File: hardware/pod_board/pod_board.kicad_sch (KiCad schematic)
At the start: 77 parts, among them J1 USB-C, J2 IMU (BNO085 breakout), J3 GNSS (NEO-M8N breakout), J4 Gesture puck (JST-GH), J5 SWD (ST-Link), J6 ELM327 fallback (USART3), J7 DB-25 to power box, SW1 RESET, SW2 BOOT, U1 STM32F405RGT6, U3 AP2112K-3.3, U4 USBLC6-2SC6, Y1 8MHz

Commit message: Power board schematic redrawn as wired sheets under a block diagram
kisheet.py writes hierarchical KiCad sheets with parts placed by hand and
wires routed between pins; power_board_drawing.py lays out eight function
sheets and the root block diagram. check.sh also builds the label-only
version and requires identical netlists (compare_nets.py).

Fixes check_nets.py reading no components from KiCad 10 netlists, which
made the footprint check pass with nothing to check.
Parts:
- removed R31, R33: 100, Resistor_SMD:R_0805_2012Metric, symbol Device:R
- removed R31, R32, R33: 1k, Resistor_SMD:R_0805_2012Metric, symbol Device:R
- removed R32: 10k, Resistor_SMD:R_0805_2012Metric, symbol Device:R
- added R31, R32, R33: 1k, Resistor_SMD:R_0805_2012Metric, symbol Device:R
- added R31, R33: 100, Resistor_SMD:R_0805_2012Metric, symbol Device:R
- added R32: 10k, Resistor_SMD:R_0805_2012Metric, symbol Device:R
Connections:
- net +3V3: now also R32.1
- net CAN_RX: now also R31.2
- net HX711_DOUT: now also R33.2
- net LED_ARMED: now also R32.1
- net LED_ARMED_A: now also R32.2
- net LED_FAULT: now also R33.1
- net LED_FAULT_A: now also R33.2
- net LED_LINK: now also R31.1
- net LED_LINK_A: now also R31.2
- net X_CAN_RX: now also R31.1, R32.2
- net X_HX711_DOUT: now also R33.1

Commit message: Pod board schematic redrawn as wired sheets; duplicate references fixed
pod_board_drawing.py draws six sheets around an MCU sheet under a block
diagram; check.sh now compares both boards' drawn and label-only netlists.
kisheet.py: stacked pins, PWR_FLAGs on signal nets, column hints for
crossing-free fan-ins, nets drawn in pieces joined by name, and visible
rail names on power symbols.

R31-R33 were used twice on the pod board, which KiCad's ERC does not
report; the netlist merged each pair. Cable parts now start at R40/C40,
generate.py rejects duplicate references and check_nets.py fails on a pin
in two nets. check_nets.py also drops the sheet path from net names.
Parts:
- removed C1, C2: 10u, Capacitor_SMD:C_1206_3216Metric, symbol Device:C
- removed C10, C11: 2.2u, Capacitor_SMD:C_0805_2012Metric, symbol Device:C
- removed C12, C13: 15p, Capacitor_SMD:C_0805_2012Metric, symbol Device:C
- removed C14, C3, C35, C4, C5, C6, C9: 100n, Capacitor_SMD:C_0805_2012Metric, symbol Device:C
- removed C15: 4.7n, Capacitor_SMD:C_0805_2012Metric, symbol Device:C
- removed C24, C27, C30: 10n, Capacitor_SMD:C_0805_2012Metric, symbol Device:C
- removed C7: 4.7u, Capacitor_SMD:C_1206_3216Metric, symbol Device:C
- removed C8: 1u, Capacitor_SMD:C_0805_2012Metric, symbol Device:C
- removed D1, D2: SS14, Diode_SMD:D_SMA, symbol Device:D_Schottky
- removed D3: green, LED_SMD:LED_0805_2012Metric, symbol Device:LED
- removed D4: blue, LED_SMD:LED_0805_2012Metric, symbol Device:LED
- removed D5: amber, LED_SMD:LED_0805_2012Metric, symbol Device:LED
- removed D6: red, LED_SMD:LED_0805_2012Metric, symbol Device:LED
- removed H1, H2, H3, H4: M3, MountingHole:MountingHole_3.2mm_M3, symbol Mechanical:MountingHole
- removed J1: USB-C, Connector_USB:USB_C_Receptacle_HRO_TYPE-C-31-M-12, symbol Connector:USB_C_Receptacle_USB2.0_16P
- removed J2: IMU (BNO085 breakout), Connector_PinHeader_2.54mm:PinHeader_1x06_P2.54mm_Vertical, symbol Connector_Generic:Conn_01x06
- removed J3: GNSS (NEO-M8N breakout), Connector_PinHeader_2.54mm:PinHeader_1x05_P2.54mm_Vertical, symbol Connector_Generic:Conn_01x05
- removed J4: Gesture puck (JST-GH), Connector_JST:JST_GH_SM05B-GHS-TB_1x05-1MP_P1.25mm_Horizontal, symbol Connector_Generic:Conn_01x05
- removed J5: SWD (ST-Link), Connector_PinHeader_2.54mm:PinHeader_1x05_P2.54mm_Vertical, symbol Connector_Generic:Conn_01x05
- removed J6: ELM327 fallback (USART3), Connector_PinHeader_2.54mm:PinHeader_1x04_P2.54mm_Vertical, symbol Connector_Generic:Conn_01x04
- removed J7: DB-25 to power box, Connector_Dsub:DSUB-25_Socket_Horizontal_P2.77x2.84mm_EdgePinOffset4.94mm_Housed_MountingHolesOffset4.94mm, symbol Connector:DB25_Socket_MountingHoles
- removed R1, R23, R26, R29, R32: 10k, Resistor_SMD:R_0805_2012Metric, symbol Device:R
- removed R10, R11, R12, R13, R14, R15, R16, R17, R18, R20, R21, R22, R25, R28, R30, R31, R32, R33, R34: 1k, Resistor_SMD:R_0805_2012Metric, symbol Device:R
- removed R19: 330, Resistor_SMD:R_0805_2012Metric, symbol Device:R
- removed R2, R3: 5.1k, Resistor_SMD:R_0805_2012Metric, symbol Device:R
- removed R31, R33: 100, Resistor_SMD:R_0805_2012Metric, symbol Device:R
- removed R36: 100k, Resistor_SMD:R_0805_2012Metric, symbol Device:R
- removed R4: 1M, Resistor_SMD:R_0805_2012Metric, symbol Device:R
- removed R5, R6: 4.7k, Resistor_SMD:R_0805_2012Metric, symbol Device:R
- removed R7, R8: 2.2k, Resistor_SMD:R_0805_2012Metric, symbol Device:R
- removed SW1: RESET, Button_Switch_SMD:SW_SPST_TL3342, symbol Switch:SW_Push
- removed SW2: BOOT, Button_Switch_SMD:SW_SPST_TL3342, symbol Switch:SW_Push
- removed U1: STM32F405RGT6, Package_QFP:LQFP-64_10x10mm_P0.5mm, symbol MCU_ST_STM32F4:STM32F405RGTx
- removed U3: AP2112K-3.3, Package_TO_SOT_SMD:SOT-23-5, symbol Regulator_Linear:AP2112K-3.3
- removed U4: USBLC6-2SC6, Package_TO_SOT_SMD:SOT-23-6, symbol Power_Protection:USBLC6-2SC6
- removed Y1: 8MHz, Crystal:Crystal_SMD_HC49-SD, symbol Device:Crystal
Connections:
- no-connect marks 15 -> 0
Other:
- added sheet Inter-box cable: DB-25, series resistors, input filters (cable.kicad_sch)
- added sheet MCU: STM32F405RGT6 (mcu.kicad_sch)
- added sheet Pod supply: USB or cable 5 V, 3.3 V regulator (power.kicad_sch)
- added sheet Sensors and local connectors (sensors.kicad_sch)
- added sheet Status LEDs (driver-facing edge) (leds.kicad_sch)
- added sheet USB-C to the laptop (usb.kicad_sch)
- note added: "WINDSCREEN POD BOARD: block diagram. Each box is a sheet (double-click it in KiCad). Power rails +3V3, VBUS and GND join the sheets by name (power symbols); every other connection between sheets is a wire here."
- note removed: "Cable line conditioning"
- note removed: "Inter-box cable (DB-25), series resistors and input filters"
- note removed: "MCU support: decoupling, crystal, reset, boot"
- note removed: "MCU: STM32F405RGT6"
- note removed: "Mounting"
- note removed: "POWER: USB VBUS OR cable +5 V -> 3.3 V"
- note removed: "Sensors and local connectors"
- note removed: "Status LEDs (driver-facing edge)"
- note removed: "USB-C to the laptop"

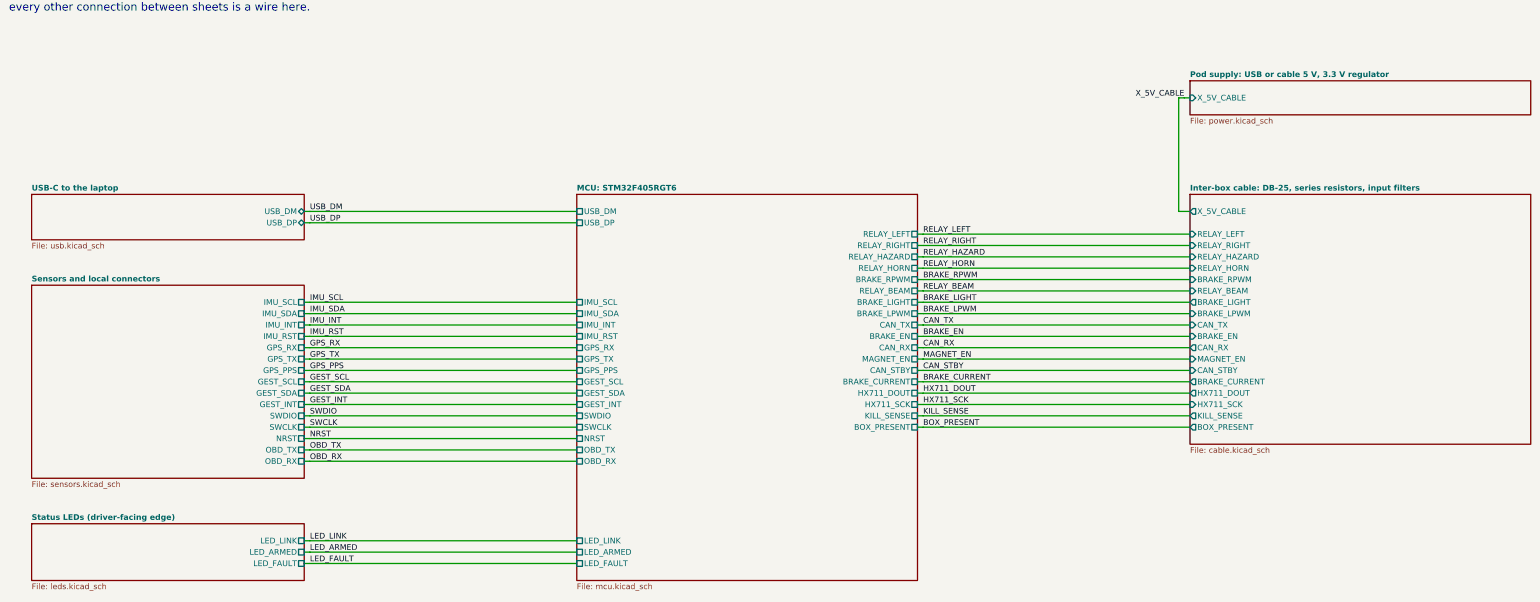
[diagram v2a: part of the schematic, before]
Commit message: PCBs routed, labelled and ready to order: Rev 1 fabrication files and buy list
Both boards placed, routed and finished by script (hardware/gen): layout.sh places
(placement.py, with silkscreen names for every terminal, port, header and button),
route.sh routes with Freerouting inside rule areas and net classes from the layout
guide and keeps a board only with 0 DRC errors, 0 unconnected and exact schematic
parity, routespec.sh checks what the DRC cannot (planes, crystal, converter loop,
IPC-2221 widths), finish.sh adds the bottom-silkscreen identification and writes
the fabrication files (gerbers, drill, BOM, positions) only when the DRC passes.

- Pod 70 x 53 mm, 4 layers: In1 solid GND, In2 +3V3, 530 teardrops; no DRC warnings.
- Power 95 x 66 mm, 2 layers, 2 oz: 10 A rail as a zone, converter re-placed (switch
  node 16 mm, feedback 7 mm, no vias; was 78 mm and 40 mm), 328 teardrops.
- Screw terminals turned to open outward; RESET/BOOT side-push on the pod's left
  edge; USB-C footprint with a 3D model (GCT USB4105).
- Pod J2 now the Adafruit 4754's JP1 row pin for pin (the old order shorted its
  3.3 V output to ground); IMU reset on a new J8; HC-05 header fed 5 V.
- Buy list per footprint and module connections in bill-of-materials.md section 10.
- LAYOUT_GUIDE rewritten as how the boards were routed and how to review them;
  decisions, progress log and BUILD_GUIDE updated; power box follows the wider board.
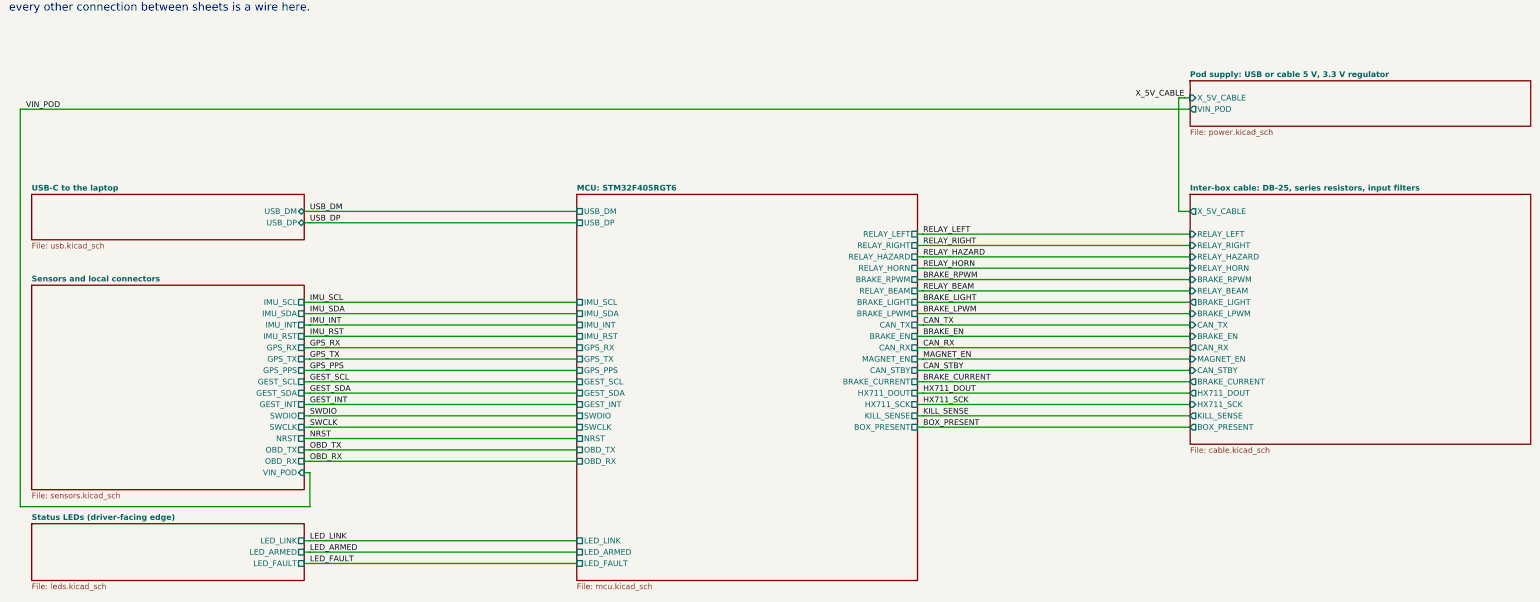
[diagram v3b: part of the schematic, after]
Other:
- sheet Pod supply: USB or cable 5 V, 3.3 V regulator ports: added VIN_POD; removed none
- sheet Sensors and local connectors ports: added VIN_POD; removed none
